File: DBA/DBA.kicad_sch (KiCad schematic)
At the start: 1 part, among them U1 ESP32_NodeMCU_v1.1

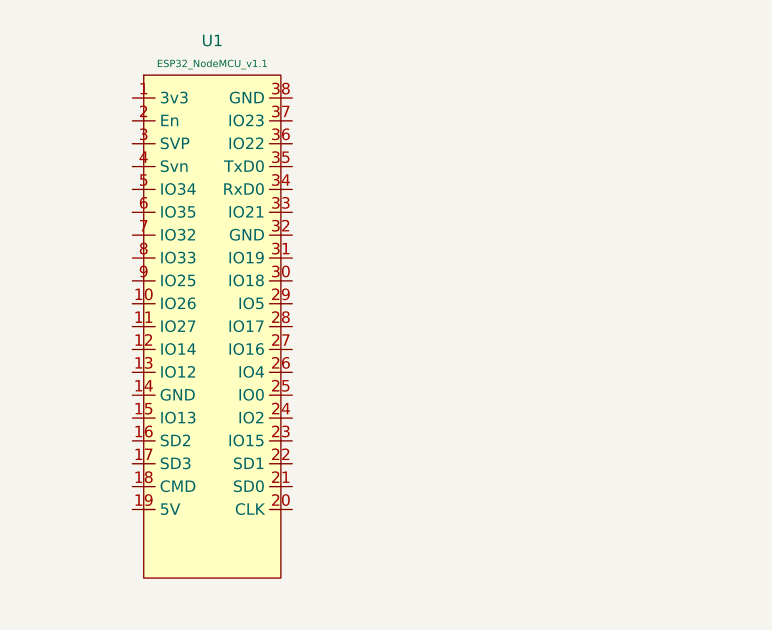
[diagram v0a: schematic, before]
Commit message: Created symbols for primary and secondary microphone
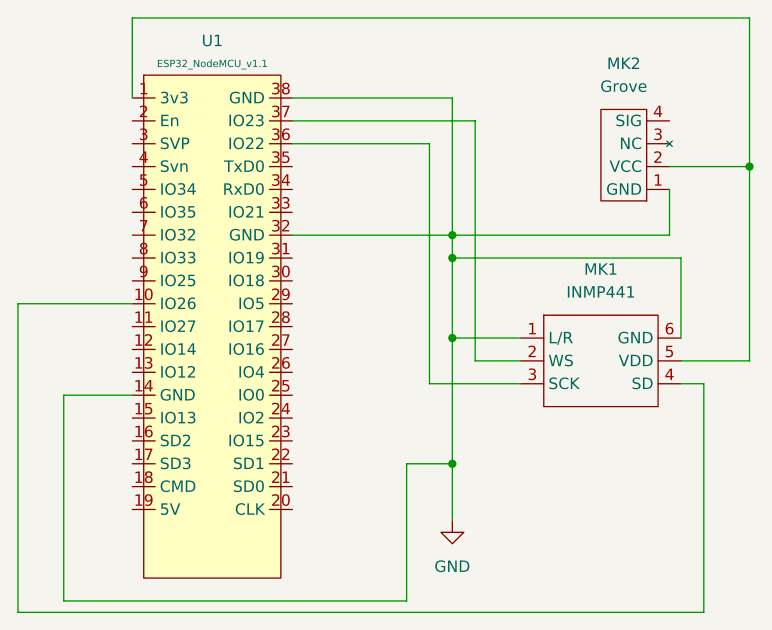
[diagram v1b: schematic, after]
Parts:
- added MK1: INMP441, Microphones:INMP441, symbol Microphone_Boards:INMP441
- added MK2: Grove, Microphones:Grove Sound Sensor, symbol Microphone_Boards:Grove
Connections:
- net at U1.1 (3v3): now also MK1.5 (VDD), MK2.2 (VCC)
- net at U1.10 (IO26): now also MK1.4 (SD)
- net GND: now reaches U1.14 (GND)
- net GND: now also U1.32 (GND), U1.38 (GND), MK1.1 (L/R), MK1.6 (GND), MK2.1 (GND)
- net at U1.36 (IO22): now also MK1.3 (SCK)
- net at U1.37 (IO23): now also MK1.2 (WS)
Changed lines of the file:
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@@
     (comment 1 "Author: Kushagra Goel")
+  )
+  (junction (at 198.12 59.69) (diameter 0) (color 0 0 0 0)
+  )
+  (junction (at 165.1 92.71) (diameter 0) (color 0 0 0 0)
+  )
+  (junction (at 165.1 67.31) (diameter 0) (color 0 0 0 0)
+  )
+  (junction (at 165.1 69.85) (diameter 0) (color 0 0 0 0)
+  )
+  (junction (at 165.1 78.74) (diameter 0) (color 0 0 0 0)
+  )
+  (wire (pts (xy 189.23 59.69) (xy 198.12 59.69))
+    (stroke (width 0) (type default) (color 0 0 0 0))
+  )
+  (wire (pts (xy 147.32 67.31) (xy 165.1 67.31))
+    (stroke (width 0) (type default) (color 0 0 0 0))
+  )
+  (wire (pts (xy 160.02 107.95) (xy 160.02 92.71))
+    (stroke (width 0) (type default) (color 0 0 0 0))
+  )
+  (wire (pts (xy 129.54 52.07) (xy 129.54 43.18))
+    (stroke (width 0) (type default) (color 0 0 0 0))
+  )
+  (wire (pts (xy 165.1 69.85) (xy 165.1 78.74))
+    (stroke (width 0) (type default) (color 0 0 0 0))
+  )
+  (wire (pts (xy 198.12 81.28) (xy 198.12 59.69))
+    (stroke (width 0) (type default) (color 0 0 0 0))
+  )
+  (wire (pts (xy 165.1 78.74) (xy 165.1 92.71))
+    (stroke (width 0) (type default) (color 0 0 0 0))
+  )
+  (wire (pts (xy 189.23 67.31) (xy 165.1 67.31))
+    (stroke (width 0) (type default) (color 0 0 0 0))
+  )
+  (wire (pts (xy 129.54 85.09) (xy 121.92 85.09))
+    (stroke (width 0) (type default) (color 0 0 0 0))
+  )
+  (wire (pts (xy 162.56 83.82) (xy 172.72 83.82))
+    (stroke (width 0) (type default) (color 0 0 0 0))
+  )
+  (wire (pts (xy 190.5 78.74) (xy 190.5 69.85))
+    (stroke (width 0) (type default) (color 0 0 0 0))
+  )
+  (wire (pts (xy 193.04 109.22) (xy 193.04 83.82))
+    (stroke (width 0) (type default) (color 0 0 0 0))
+  )
+  (wire (pts (xy 167.64 81.28) (xy 167.64 54.61))
+    (stroke (width 0) (type default) (color 0 0 0 0))
+  )
+  (wire (pts (xy 121.92 107.95) (xy 160.02 107.95))
+    (stroke (width 0) (type default) (color 0 0 0 0))
+  )
+  (wire (pts (xy 116.84 74.93) (xy 116.84 109.22))
+    (stroke (width 0) (type default) (color 0 0 0 0))
+  )
+  (wire (pts (xy 116.84 109.22) (xy 193.04 109.22))
+    (stroke (width 0) (type default) (color 0 0 0 0))
+  )
+  (wire (pts (xy 121.92 85.09) (xy 121.92 107.95))
+    (stroke (width 0) (type default) (color 0 0 0 0))
+  )
+  (wire (pts (xy 172.72 81.28) (xy 167.64 81.28))
+    (stroke (width 0) (type default) (color 0 0 0 0))
+  )
+  (wire (pts (xy 129.54 74.93) (xy 116.84 74.93))
+    (stroke (width 0) (type default) (color 0 0 0 0))
+  )
+  (wire (pts (xy 129.54 43.18) (xy 198.12 43.18))
+    (stroke (width 0) (type default) (color 0 0 0 0))
+  )
+  (wire (pts (xy 165.1 78.74) (xy 172.72 78.74))
+    (stroke (width 0) (type default) (color 0 0 0 0))
+  )
+  (wire (pts (xy 190.5 81.28) (xy 198.12 81.28))
+    (stroke (width 0) (type default) (color 0 0 0 0))
+  )
+  (wire (pts (xy 198.12 43.18) (xy 198.12 59.69))
+    (stroke (width 0) (type default) (color 0 0 0 0))
+  )
+  (wire (pts (xy 165.1 69.85) (xy 190.5 69.85))
+    (stroke (width 0) (type default) (color 0 0 0 0))
+  )
+  (wire (pts (xy 147.32 52.07) (xy 165.1 52.07))
+    (stroke (width 0) (type default) (color 0 0 0 0))
+  )
+  (wire (pts (xy 165.1 92.71) (xy 165.1 99.06))
+    (stroke (width 0) (type default) (color 0 0 0 0))
+  )
+  (wire (pts (xy 165.1 67.31) (xy 165.1 69.85))
+    (stroke (width 0) (type default) (color 0 0 0 0))
+  )
+  (wire (pts (xy 160.02 92.71) (xy 165.1 92.71))
+    (stroke (width 0) (type default) (color 0 0 0 0))
+  )
+  (wire (pts (xy 162.56 57.15) (xy 162.56 83.82))
+    (stroke (width 0) (type default) (color 0 0 0 0))
+  )
+  (wire (pts (xy 147.32 54.61) (xy 167.64 54.61))
+    (stroke (width 0) (type default) (color 0 0 0 0))
+  )
+  (wire (pts (xy 193.04 83.82) (xy 190.5 83.82))
+    (stroke (width 0) (type default) (color 0 0 0 0))
+  )
+  (wire (pts (xy 147.32 57.15) (xy 162.56 57.15))
+    (stroke (width 0) (type default) (color 0 0 0 0))
+  )
+  (wire (pts (xy 189.23 62.23) (xy 189.23 67.31))
+    (stroke (width 0) (type default) (color 0 0 0 0))
+  )
+  (wire (pts (xy 165.1 52.07) (xy 165.1 67.31))
+    (stroke (width 0) (type default) (color 0 0 0 0))
+  )
+  (symbol (lib_id "Microphone_Boards:INMP441") (at 181.61 81.28 0) (unit 1)
+    (in_bom yes) (on_board yes) (fields_autoplaced)
+    (property "Reference" "MK1" (id 0) (at 181.61 71.12 0))
+    (property "Value" "INMP441" (id 1) (at 181.61 73.66 0))
+    (property "Footprint" "Microphones:INMP441" (id 2) (at 180.34 81.28 0)
+      (effects (font (size 1.27 1.27)) hide)
+    )
+    (property "Datasheet" "" (id 3) (at 180.34 81.28 0)
+      (effects (font (size 1.27 1.27)) hide)
+    )
+    (pin "1")
+    (pin "2")
+    (pin "3")
+    (pin "4")
+    (pin "5")
+    (pin "6")
   )
   (symbol (lib_id "MCU_Espressif:ESP32_NodeMCU_v1.1") (at 138.43 78.74 0) (unit 1)
@@
     (pin "9")
   )
+  (symbol (lib_id "Microphone_Boards:Grove") (at 184.15 60.96 180) (unit 1)
+    (in_bom yes) (on_board yes) (fields_autoplaced)
+    (property "Reference" "MK2" (id 0) (at 184.15 48.26 0))
+    (property "Value" "Grove" (id 1) (at 184.15 50.8 0))
+    (property "Footprint" "Microphones:Grove Sound Sensor" (id 2) (at 182.88 52.07 0)
+      (effects (font (size 1.27 1.27)) hide)
+    )
+    (property "Datasheet" "" (id 3) (at 191.77 59.69 0)
+      (effects (font (size 1.27 1.27)) hide)
+    )
+    (pin "2")
+    (pin "3")
+    (pin "4")
+    (pin "1")
+  )
+  (symbol (lib_id "power:GND") (at 165.1 99.06 0) (unit 1)
+    (in_bom yes) (on_board yes) (fields_autoplaced)
+    (property "Reference" "#PWR0101" (id 0) (at 165.1 105.41 0)
+      (effects (font (size 1.27 1.27)) hide)
+    )
+    (property "Value" "GND" (id 1) (at 165.1 104.14 0))
+    (property "Footprint" "" (id 2) (at 165.1 99.06 0)
+      (effects (font (size 1.27 1.27)) hide)
+    )
+    (property "Datasheet" "" (id 3) (at 165.1 99.06 0)
+      (effects (font (size 1.27 1.27)) hide)
+    )
+    (pin "1")
+  )
   (sheet_instances
     (path "/" (page "1"))
   )
   (symbol_instances
+    (path "/cf71bbe1-28d7-4f38-852d-04a11ad22d15"
+      (reference "#PWR0101") (unit 1) (value "GND") (footprint "")
+    )
+    (path "/3fe36949-2a99-4cf8-820d-261441682873"
+      (reference "MK1") (unit 1) (value "INMP441") (footprint "Microphones:INMP441")
+    )
+    (path "/a93081a0-35bb-4572-ba64-487dc306631c"
+      (reference "MK2") (unit 1) (value "Grove") (footprint "Microphones:Grove Sound Sensor")
+    )
     (path "/a2a97bd8-d497-44f7-8dec-0b4beac24896"
       (reference "U1") (unit 1) (value "ESP32_NodeMCU_v1.1") (footprint "Package_DIP:DIP-38_W22.86mm")

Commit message: First complete model
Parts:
- added A1: TP4056, custom:TP4056Board, symbol Battery_Management:TP4056
- added BT1: Battery_Cell, Battery:BatteryHolder_Keystone_1042_1x18650, symbol Device:Battery_Cell
- added C1: 100n, Capacitor_THT:C_Radial_D6.3mm_H5.0mm_P2.50mm, symbol Device:C
- added C2: 100u, Capacitor_THT:CP_Radial_D5.0mm_P2.50mm, symbol Device:C_Polarized
- added J1: USB_B_Micro, symbol Connector:USB_B_Micro
- added J4, J5: Conn_01x01_Male, Connector_PinHeader_2.54mm:PinHeader_1x01_P2.54mm_Vertical, symbol Connector:Conn_01x01_Male
- added U2: MCP1700-3302E_TO92, Package_TO_SOT_THT:TO-92_Inline, symbol Regulator_Linear:MCP1700-3302E_TO92
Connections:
- net GND: now also C1.1, C2.2, J5.1 (Pin_1), U2.1 (GND)
- net at MK1.5 (VDD), MK2.2 (VCC), U1.1 (3v3): now also C1.2, C2.1, U2.3 (VO)
- net at U1.9 (IO25): now also MK2.4 (SIG)
- new net: J4.1 (Pin_1), U2.2 (VI)
- new net: A1.1 (IN+), J1.1 (VBUS)
- new net: A1.2 (IN-), J1.5 (GND)
- no-connect marks 0 -> 4
